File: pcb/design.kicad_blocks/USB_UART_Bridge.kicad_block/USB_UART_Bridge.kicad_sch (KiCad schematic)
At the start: 16 parts, among them J1 614105150721, U2 MCP2221A-I/ST, U3 AP2112K-3.3

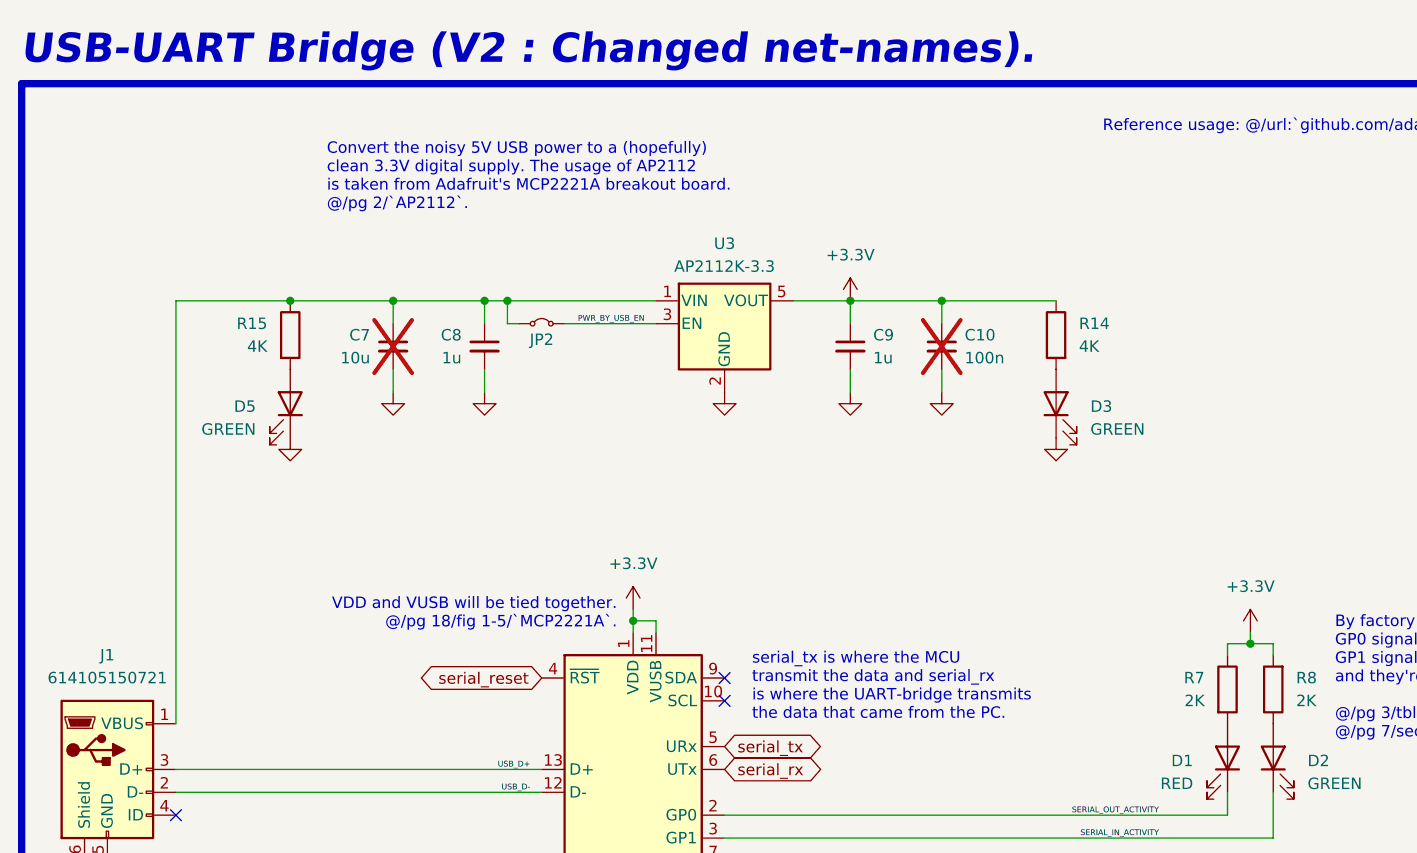
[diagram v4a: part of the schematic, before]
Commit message: Added pull-up for reset pin of MCP2221A.
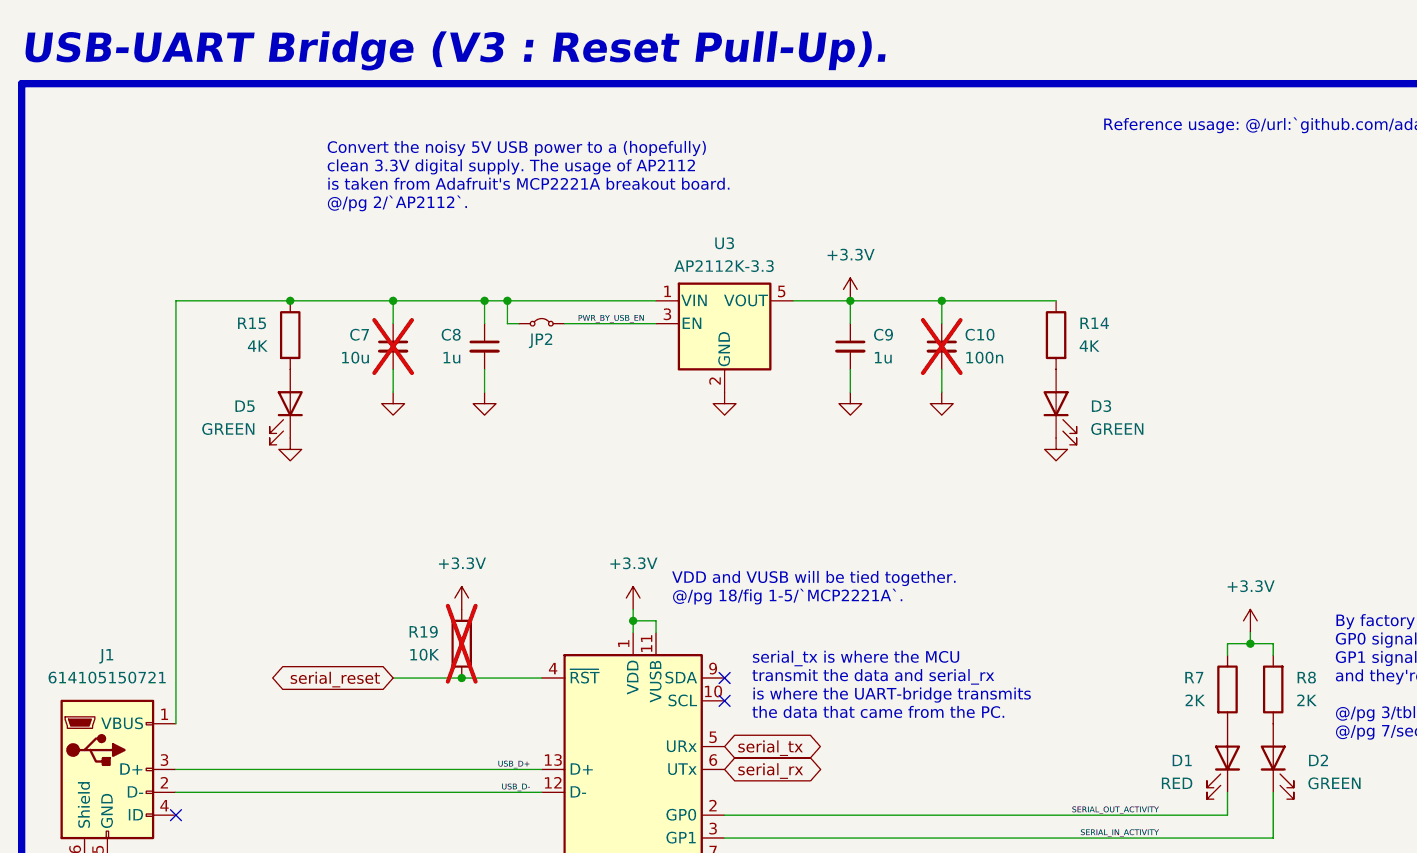
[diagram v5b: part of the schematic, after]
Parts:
- added R19: 10K, Resistor_SMD:R_1206_3216Metric_Pad1.30x1.75mm_HandSolder, symbol Device:R
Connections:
- net +3.3V: now also R19.1
- net serial_reset: now also R19.2
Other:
- note added: "USB-UART Bridge (V3 : Reset Pull-Up)."
- note removed: "USB-UART Bridge (V2 : Changed net-names)."
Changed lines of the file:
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@@
 		)
 	)
-	(text "USB-UART Bridge (V2 : Changed net-names)."
+	(text "USB-UART Bridge (V3 : Reset Pull-Up)."
 		(exclude_from_sim no)
 		(at 314.198 85.852 0)
@@
 	(text "VDD and VUSB will be tied together.\n@/pg 18/fig 1-5/`MCP2221A`."
 		(exclude_from_sim no)
-		(at 380.492 148.336 0)
+		(at 386.588 145.542 0)
 		(effects
 			(font
@@
 				(color 255 0 0 1)
 			)
-			(justify right bottom)
+			(justify left bottom)
 		)
 	)
@@
 	)
 	(junction
+		(at 363.22 153.67)
+		(diameter 0)
+		(color 0 0 0 0)
+	)
+	(junction
 		(at 416.56 111.76)
 		(diameter 0)
@@
 	(wire
 		(pts
+			(xy 355.6 153.67) (xy 363.22 153.67)
+		)
+		(stroke
+			(width 0)
+			(type default)
+		)
+	)
+	(wire
+		(pts
 			(xy 331.47 163.83) (xy 372.11 163.83)
 		)
@@
 		(pts
 			(xy 355.6 121.92) (xy 355.6 119.38)
+		)
+		(stroke
+			(width 0)
+			(type default)
+		)
+	)
+	(wire
+		(pts
+			(xy 363.22 153.67) (xy 372.11 153.67)
 		)
 		(stroke
@@
 	(global_label "serial_reset"
 		(shape bidirectional)
-		(at 372.11 153.67 180)
+		(at 355.6 153.67 180)
 		(fields_autoplaced yes)
 		(effects
@@
 		)
 		(property "Intersheetrefs" "${INTERSHEET_REFS}"
-			(at 357.0068 153.67 0)
+			(at 340.4968 153.67 0)
 			(effects
 				(font
@@
 	)
 	(symbol
+		(lib_id "power:+3.3V")
+		(at 363.22 146.05 0)
+		(unit 1)
+		(exclude_from_sim no)
+		(in_bom yes)
+		(on_board yes)
+		(dnp no)
+		(fields_autoplaced yes)
+		(property "Reference" "#PWR052"
+			(at 363.22 149.86 0)
+			(effects
+				(font
+					(size 1.27 1.27)
+				)
+				(hide yes)
+			)
+		)
+		(property "Value" "+3.3V"
+			(at 363.22 140.97 0)
+			(effects
+				(font
+					(size 1.27 1.27)
+				)
+			)
+		)
+		(property "Footprint" ""
+			(at 363.22 146.05 0)
+			(effects
+				(font
+					(size 1.27 1.27)
+				)
+				(hide yes)
+			)
+		)
+		(property "Datasheet" ""
+			(at 363.22 146.05 0)
+			(effects
+				(font
+					(size 1.27 1.27)
+				)
+				(hide yes)
+			)
+		)
+		(property "Description" "Power symbol creates a global label with name \"+3.3V\""
+			(at 363.22 146.05 0)
+			(effects
+				(font
+					(size 1.27 1.27)
+				)
+				(hide yes)
+			)
+		)
+		(pin "1"
+		)
+		(instances
+			(project "MainFlightComputer"
+				(path "/0a179c33-cb18-4019-99e7-0e00d41f97d6"
+					(reference "#PWR052")
+					(unit 1)
+				)
+			)
+		)
+	)
+	(symbol
 		(lib_id "Device:R")
 		(at 429.26 115.57 0)
@@
 					(unit 1)
 				)
+			)
+		)
+	)
+	(symbol
+		(lib_id "Device:R")
+		(at 363.22 149.86 0)
+		(unit 1)
+		(exclude_from_sim no)
+		(in_bom yes)
+		(on_board yes)
+		(dnp yes)
+		(property "Reference" "R19"
+			(at 360.68 148.5899 0)
+			(effects
+				(font
+					(size 1.27 1.27)
+				)
+				(justify right)
+			)
+		)
+		(property "Value" "10K"
+			(at 360.68 151.1299 0)
+			(effects
+				(font
+					(size 1.27 1.27)
+				)
+				(justify right)
+			)
+		)
+		(property "Footprint" "Resistor_SMD:R_1206_3216Metric_Pad1.30x1.75mm_HandSolder"
+			(at 361.442 149.86 90)
+			(effects
+				(font
+					(size 1.27 1.27)
+				)
+				(hide yes)
+			)
+		)
+		(property "Datasheet" "~"
+			(at 363.22 149.86 0)
+			(effects
+				(font
+					(size 1.27 1.27)
+				)
+				(hide yes)
+			)
+		)
+		(property "Description" "Resistor"
+			(at 363.22 149.86 0)
+			(effects
+				(font
+					(size 1.27 1.27)
+				)
+				(hide yes)
+			)
+		)
+		(pin "1"
+		)
+		(pin "2"
+		)
+		(instances
+			(project "MainFlightComputer"
+				(path "/0a179c33-cb18-4019-99e7-0e00d41f97d6"
+					(reference "R19")
+					(unit 1)
+				)

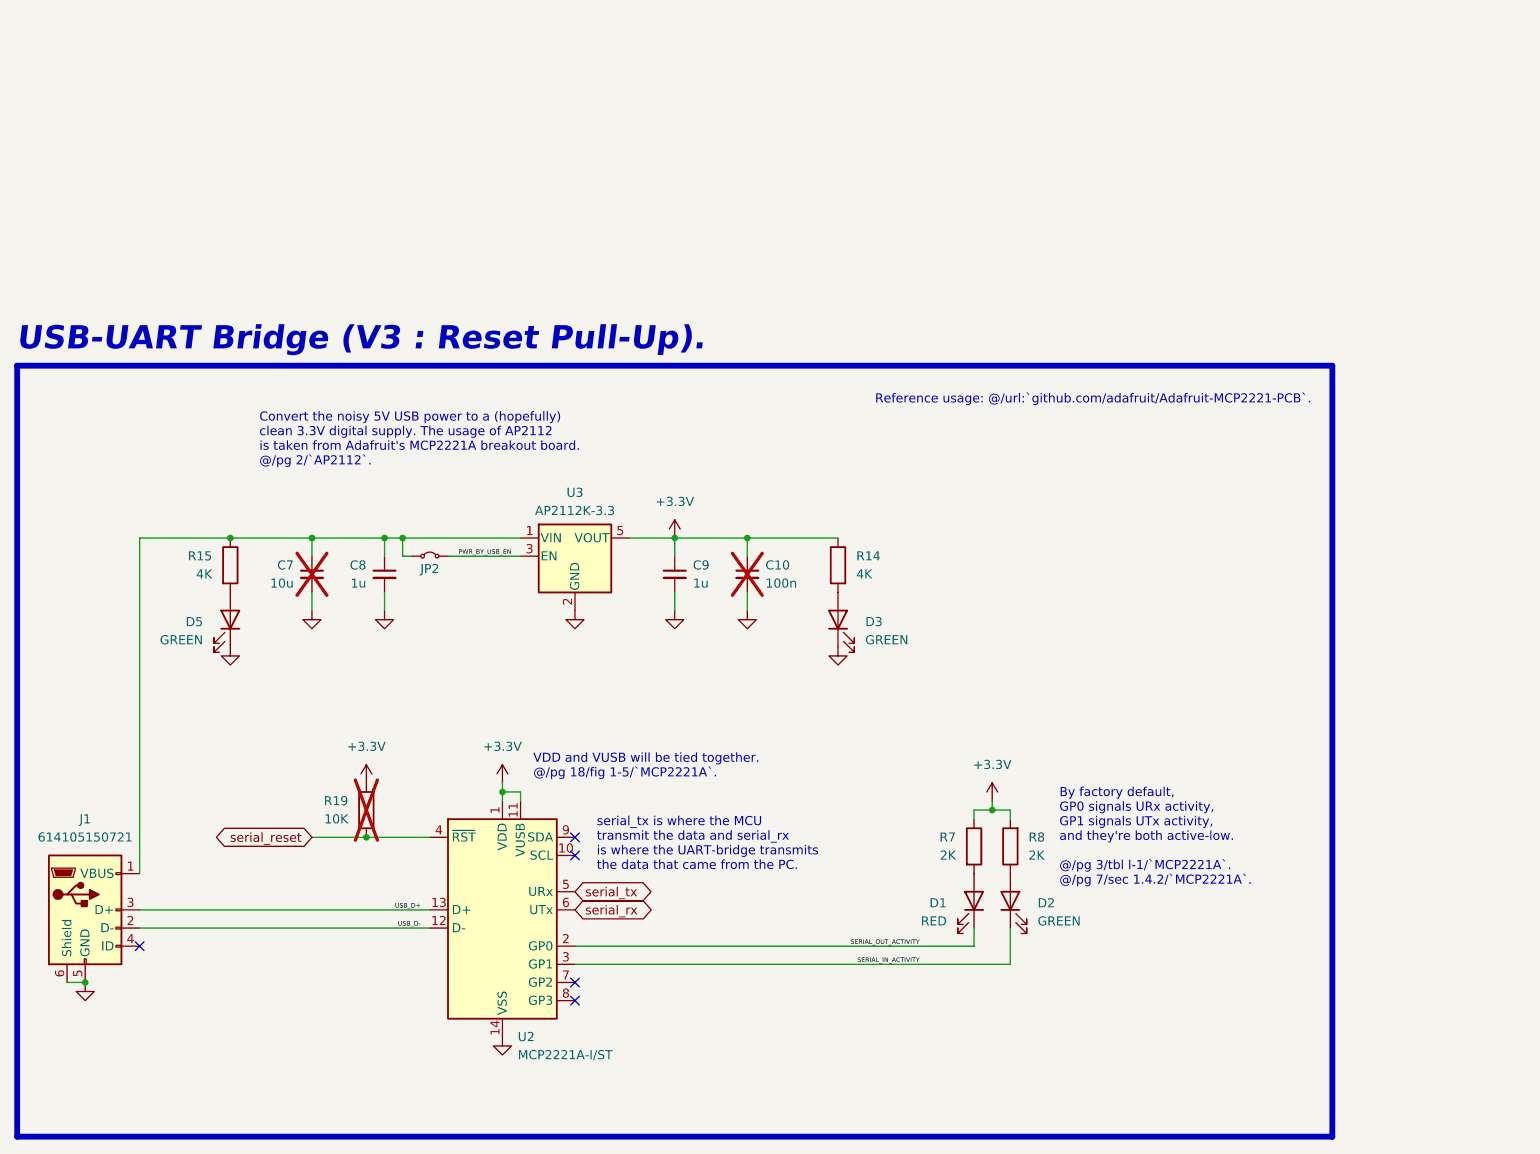
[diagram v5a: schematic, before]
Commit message: Beginning placements of some components.
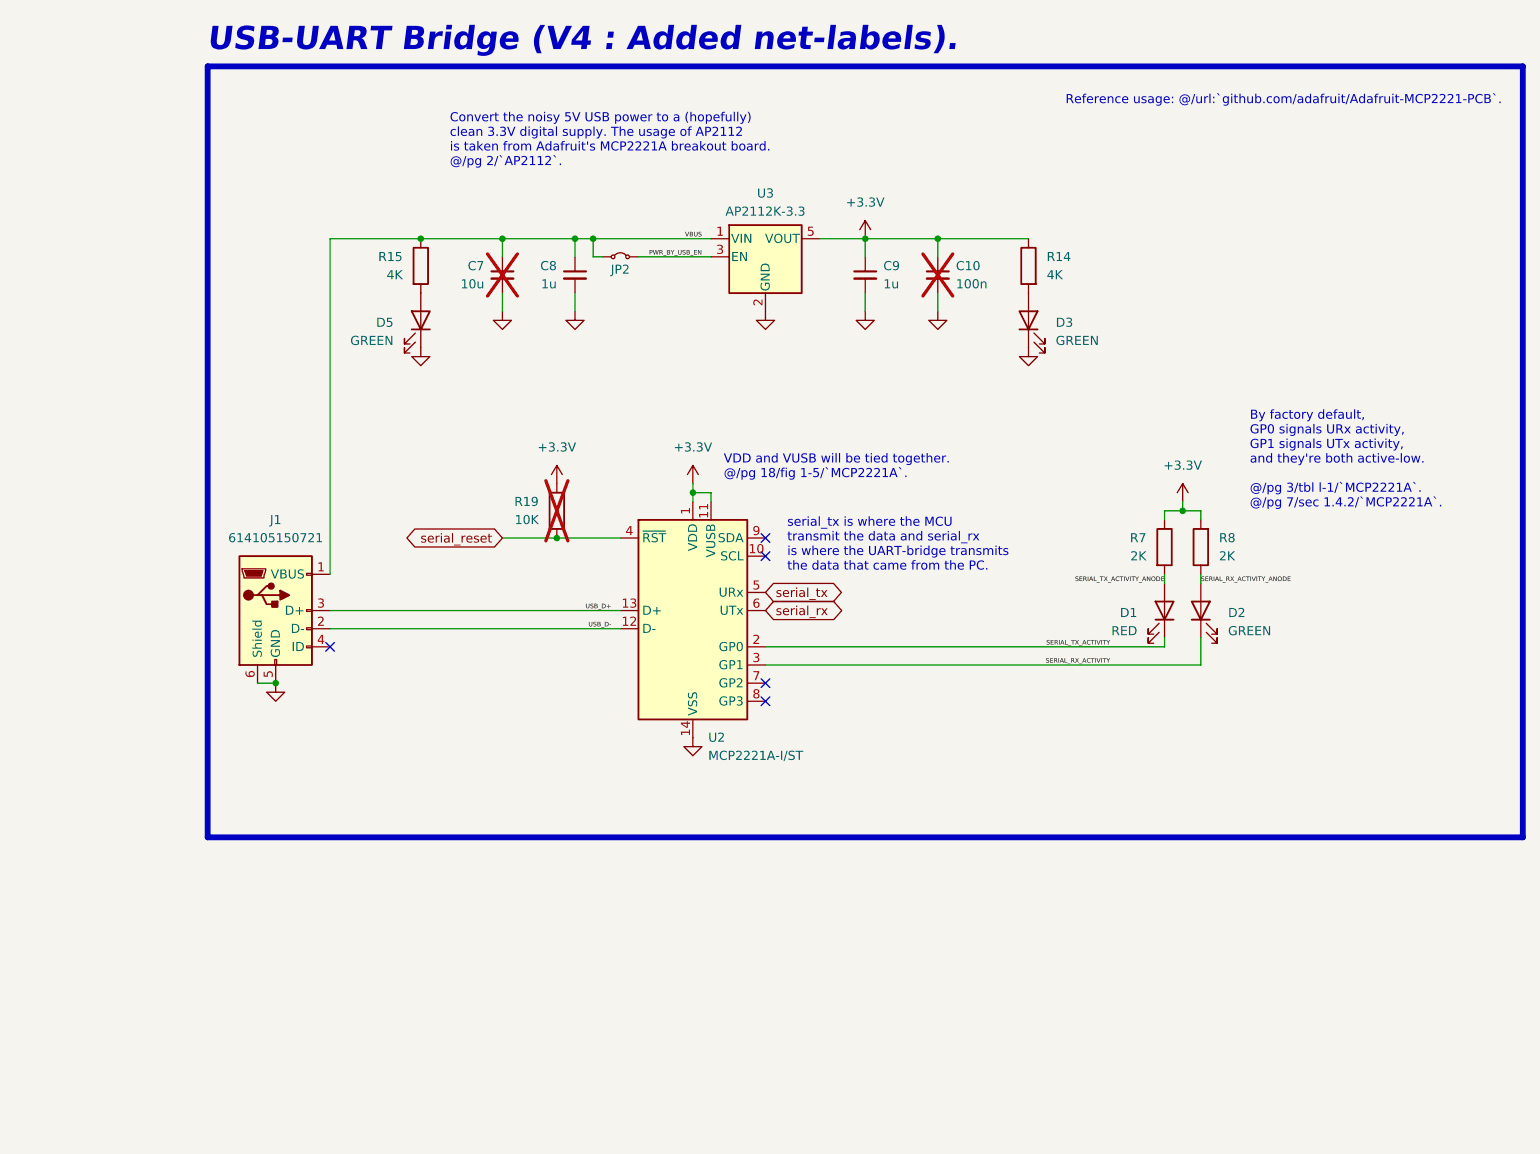
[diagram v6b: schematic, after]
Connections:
- net VBUS: now reaches C7.1, C8.1, J1.1 (VBUS), JP2.1 (A), R15.1, U3.1 (VIN)
- net SERIAL_RX_ACTIVITY_ANODE: now reaches D2.2 (A), R8.1
- net SERIAL_TX_ACTIVITY_ANODE: now reaches D1.2 (A), R7.2
- net SERIAL_IN_ACTIVITY renamed SERIAL_RX_ACTIVITY
- net SERIAL_OUT_ACTIVITY renamed SERIAL_TX_ACTIVITY
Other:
- note added: "USB-UART Bridge (V4 : Added net-labels)."
- note removed: "USB-UART Bridge (V3 : Reset Pull-Up)."
- moved on the sheet: C10, C7, C8, C9, D1, D2, D3, D5, J1, JP2, R14, R15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
